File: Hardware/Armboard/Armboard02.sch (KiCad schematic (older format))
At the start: 0 parts

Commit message: H-Bridge completed
Completed the H-Bridge Hierarchal Sheet
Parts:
- added C1: 33nF, symbol Device:C_Small
- added Conn? (x2): AndersonPP, symbol MRDT_Connectors:AndersonPP
- added D1: Zener, symbol Device:D_Zener
- added Gripper_Motor: VNH5019A_E, symbol MRDT_ICs:VNH5019A_E
- added R1, R2, R4, R6, R7, R8: 1k, symbol Device:R
- added R3: 0, symbol Device:R
- added R5: 10k, symbol Device:R
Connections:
- new net: Gripper_Motor.10 (IN_B), R8.2
- new net: Gripper_Motor.4 (IN_A), R1.2
- new net: Gripper_Motor.5 (EN_A/DIAG_A), R2.2
- new net: Gripper_Motor.6 (CS_DIS), R3.2
- new net: Gripper_Motor.7 (PWM), R4.2
- new net: Gripper_Motor.8 (CS), R5.2, R6.1
- new net: Gripper_Motor.9 (EN_B/DIAG_B), R7.2
- new net +12VA: Gripper_Motor.12 (V_BAT), Gripper_Motor.13 (VCC), Gripper_Motor.23 (VCC), Gripper_Motor.3 (VCC), Gripper_Motor.32 (VCC_HEATSLUG)
- new net +3V3: R2.1, R3.1, R7.1
- new net GND: C1.2, D1.2 (A), Gripper_Motor.18 (GND), Gripper_Motor.19 (GND), Gripper_Motor.20 (GND), Gripper_Motor.26 (GND), Gripper_Motor.27 (GND), Gripper_Motor.28 (GND), R6.2
- new net IN_A: R1.1, R8.1
- new net I_SENSE: C1.1, D1.1 (K), R5.1
- new net M_PWM: R4.1
- new net Out_A_M: Conn?.2 (V+Log), Gripper_Motor.1 (OUT_A), Gripper_Motor.25 (OUT_A), Gripper_Motor.30 (OUT_A), Gripper_Motor.31 (OUT_A_HEATSLUG)
- new net Out_B_M: Conn?.1 (GND), Gripper_Motor.15 (OUT_B), Gripper_Motor.16 (OUT_B), Gripper_Motor.21 (OUT_B), Gripper_Motor.33 (OUT_B_HEATSLUG)

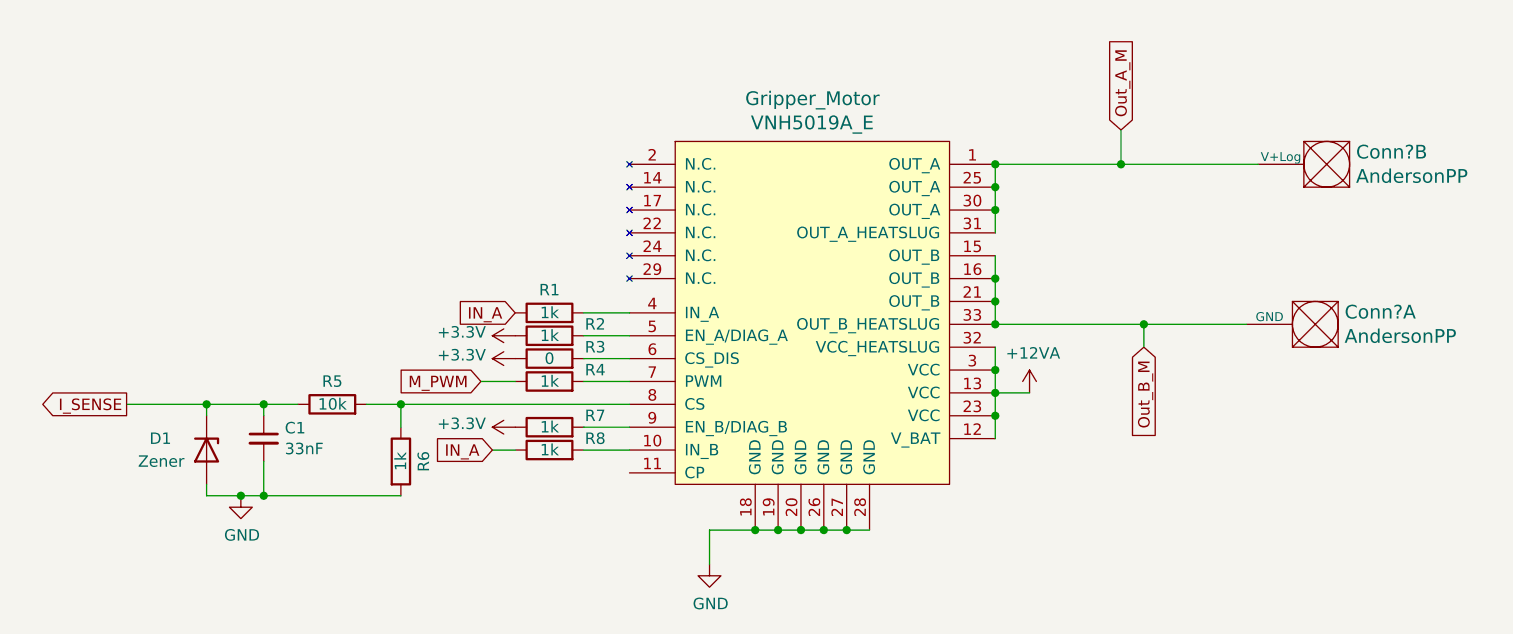
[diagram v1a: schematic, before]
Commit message: Updated H-Bridge
Made the appropriate changes suggested by anthony in slack chat regarding the H-Bridge's flaws
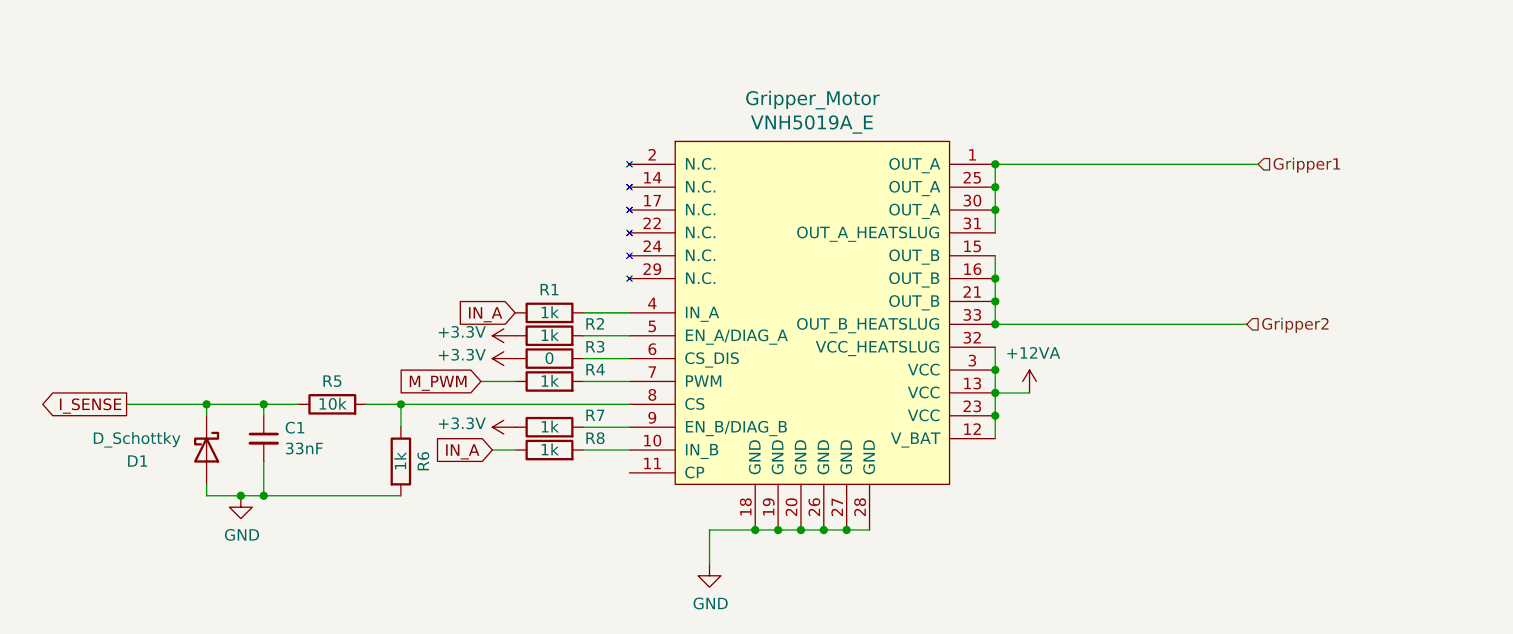
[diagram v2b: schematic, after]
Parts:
- removed Conn? (x2): AndersonPP, symbol MRDT_Connectors:AndersonPP
- removed D1: Zener, symbol Device:D_Zener
- added D_Schottky: D1, symbol Device:D_Schottky
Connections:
- net GND: now also D_Schottky.2 (A)
- net I_SENSE: now also D_Schottky.1 (K)
- net Out_A_M renamed Gripper1
- net Out_B_M renamed Gripper2
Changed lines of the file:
@@
 Wire Wire Line
 	6100 2350 6100 2450
-Wire Wire Line
-	6100 2150 6650 2150
 Connection ~ 6100 2150
 Wire Wire Line
@@
 Wire Wire Line
 	6100 2750 6100 2850
-Wire Wire Line
-	6100 2850 6750 2850
-Connection ~ 6100 2850
 Wire Wire Line
 	6100 2950 6100 3050
@@
 	1    0    0    -1
 $EndComp
-Text GLabel 6650 2000 1    50   Input ~ 0
-Out_A_M
-Wire Wire Line
-	6650 2000 6650 2150
-Connection ~ 6650 2150
-Wire Wire Line
-	6650 2150 7250 2150
-$Comp
-L MRDT_Connectors:AndersonPP Conn?
-U 2 1 5F7FDECE
-P 7650 2250
-F 0 "Conn?" H 7622 2403 60  0000 R CNN
-F 1 "AndersonPP" H 7622 2297 60  0000 R CNN
-F 2 "" H 7500 1700 60  0001 C CNN
-F 3 "" H 7500 1700 60  0001 C CNN
-	2    7650 2250
-	-1   0    0    -1
-$EndComp
-$Comp
-L MRDT_Connectors:AndersonPP Conn?
-U 1 1 5F7FEB3C
-P 7600 2950
-F 0 "Conn?" H 7572 3103 60  0000 R CNN
-F 1 "AndersonPP" H 7572 2997 60  0000 R CNN
-F 2 "" H 7450 2400 60  0001 C CNN
-F 3 "" H 7450 2400 60  0001 C CNN
-	1    7600 2950
-	-1   0    0    -1
-$EndComp
-Text GLabel 6750 2950 3    50   Input ~ 0
-Out_B_M
-Wire Wire Line
-	6750 2950 6750 2850
-Connection ~ 6750 2850
-Wire Wire Line
-	6750 2850 7200 2850
 Wire Wire Line
 	4500 2800 4300 2800
@@
 Wire Wire Line
 	4300 3100 4500 3100
-Text GLabel 3850 3100 0    50   Input ~ 0
-M_PWM
-Text GLabel 4000 2800 0    50   Input ~ 0
-IN_A
 $Comp
 L Device:R R5
@@
 	2650 3600 2650 3550
 Connection ~ 2800 3600
-$Comp
-L Device:D_Zener D1
-U 1 1 5F80F516
-P 2650 3400
-F 0 "D1" V 2600 3150 50  0000 L CNN
-F 1 "Zener" V 2700 3100 50  0000 L CNN
-F 2 "" H 2650 3400 50  0001 C CNN
-F 3 "~" H 2650 3400 50  0001 C CNN
-	1    2650 3400
-	0    1    1    0
-$EndComp
 Text GLabel 2300 3200 0    50   Output ~ 0
 I_SENSE
@@
 	0    -1   -1   0
 $EndComp
+Wire Wire Line
+	3500 3200 4500 3200
+$Comp
+L Device:D_Schottky D_Schottky
+U 1 1 5F84D0E8
+P 2650 3400
+F 0 "D_Schottky" V 2600 2900 50  0000 L CNN
+F 1 "D1" V 2700 3050 50  0000 L CNN
+F 2 "" H 2650 3400 50  0001 C CNN
+F 3 "~" H 2650 3400 50  0001 C CNN
+	1    2650 3400
+	0    1    1    0
+$EndComp
+Wire Wire Line
+	6100 2150 7250 2150
+Connection ~ 6100 2850
+Wire Wire Line
+	6100 2850 7200 2850
+Wire Wire Line
+	3850 3100 4000 3100
+Wire Wire Line
+	4000 3400 3900 3400
 Text GLabel 3900 3400 0    50   Input ~ 0
 IN_A
-Wire Wire Line
-	3500 3200 4500 3200
-Wire Wire Line
-	3850 3100 4000 3100
-Wire Wire Line
-	4000 3400 3900 3400
+Text GLabel 4000 2800 0    50   Input ~ 0
+IN_A
+Text GLabel 3850 3100 0    50   Input ~ 0
+M_PWM
+Text HLabel 7250 2150 2    50   Input ~ 0
+Gripper1
+Text HLabel 7200 2850 2    50   Input ~ 0
+Gripper2
 $EndSCHEMATC

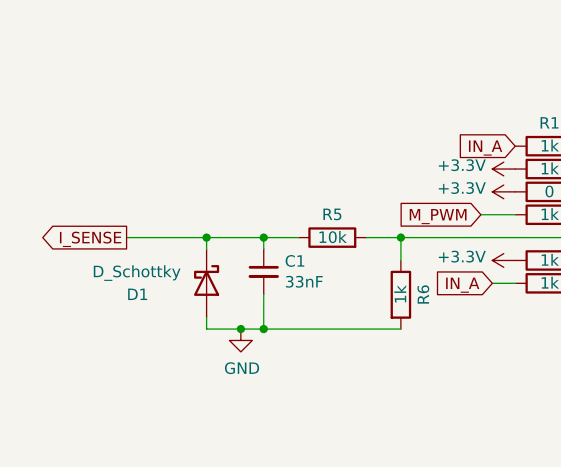
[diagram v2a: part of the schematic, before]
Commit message: Zener fix
Replaced the schotkey diode or however you spell it, with the zener diode
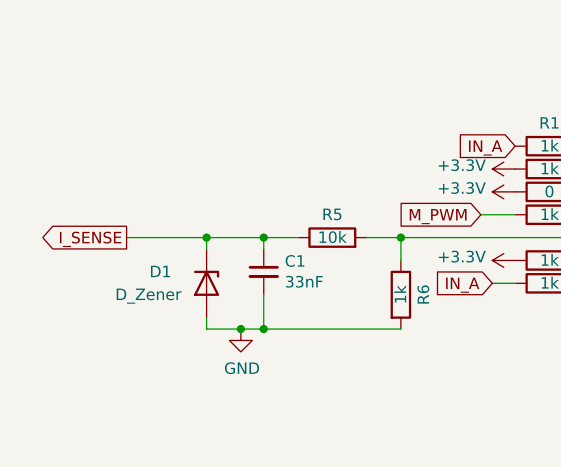
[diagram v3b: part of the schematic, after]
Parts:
- removed D_Schottky: D1, symbol Device:D_Schottky
- added D1: D_Zener, symbol Device:D_Zener
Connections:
- net GND: now also D1.2 (A)
- net I_SENSE: now also D1.1 (K)
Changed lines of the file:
@@
 Wire Wire Line
 	3500 3200 4500 3200
-$Comp
-L Device:D_Schottky D_Schottky
-U 1 1 5F84D0E8
-P 2650 3400
-F 0 "D_Schottky" V 2600 2900 50  0000 L CNN
-F 1 "D1" V 2700 3050 50  0000 L CNN
-F 2 "" H 2650 3400 50  0001 C CNN
-F 3 "~" H 2650 3400 50  0001 C CNN
-	1    2650 3400
-	0    1    1    0
-$EndComp
 Wire Wire Line
 	6100 2150 7250 2150
@@
 Text HLabel 7200 2850 2    50   Input ~ 0
 Gripper2
+$Comp
+L Device:D_Zener D1
+U 1 1 5F8E563D
+P 2650 3400
+F 0 "D1" V 2600 3150 50  0000 L CNN
+F 1 "D_Zener" V 2700 3000 50  0000 L CNN
+F 2 "" H 2650 3400 50  0001 C CNN
+F 3 "~" H 2650 3400 50  0001 C CNN
+	1    2650 3400
+	0    1    1    0
+$EndComp
 $EndSCHEMATC

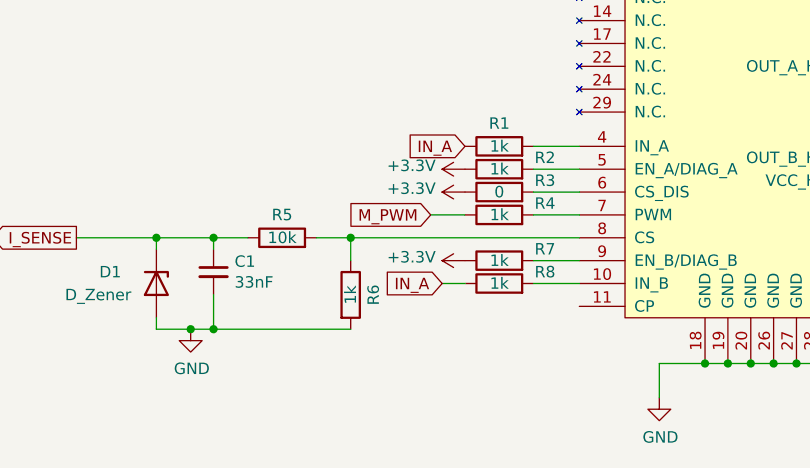
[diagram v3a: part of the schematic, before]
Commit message: Review 2 board changes
-Connected the busses on the power and H-Bridge
-Changed the resistor value to 1.2k
-Fixed some of the pin locations on the TIVA
-Added ferrites to the H-Bridge
-Connected the buses so that they all highlight correctly
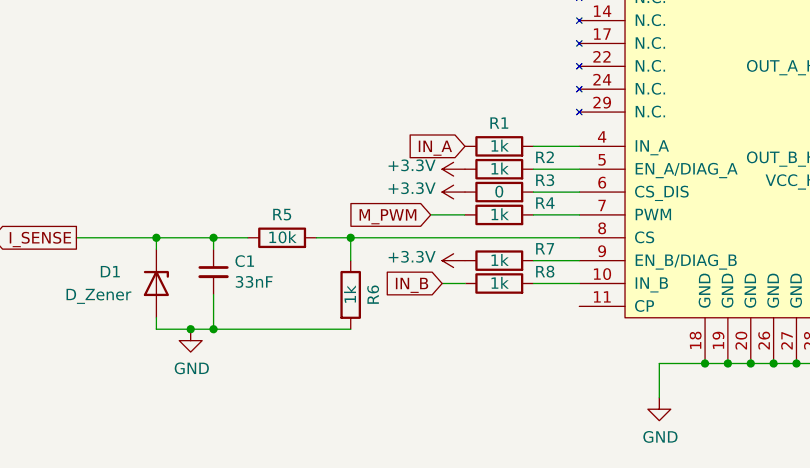
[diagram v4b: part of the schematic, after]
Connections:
- net IN_A: no longer R8.1
- new net IN_B: R8.1
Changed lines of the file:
@@
 $Descr A 11000 8500
 encoding utf-8
-Sheet 3 9
+Sheet 9 9
 Title ""
 Date ""
@@
 	4000 3400 3900 3400
 Text GLabel 3900 3400 0    50   Input ~ 0
-IN_A
+IN_B
 Text GLabel 4000 2800 0    50   Input ~ 0
 IN_A

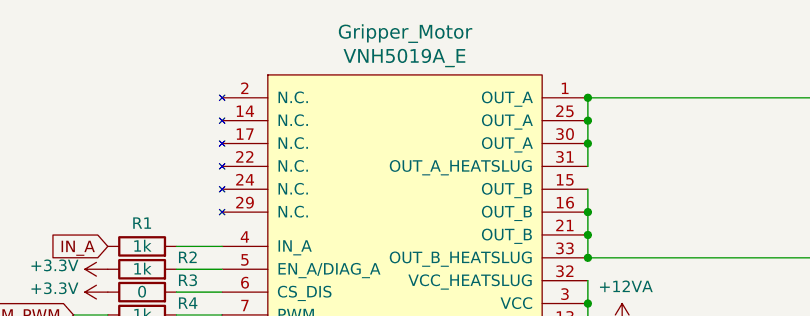
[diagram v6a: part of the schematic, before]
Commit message: Assigned R/L/C footprints
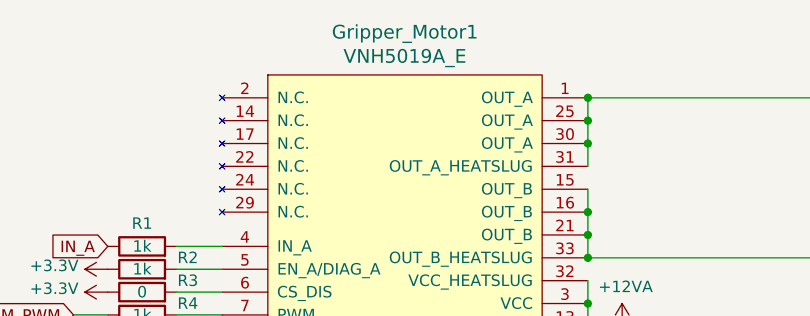
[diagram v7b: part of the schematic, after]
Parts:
- C1: footprint (none) -> Capacitor_SMD:C_0603_1608Metric_Pad1.05x0.95mm_HandSolder
- R1, R2, R3, R4, R5, R6, R7, R8: footprint (none) -> Resistor_SMD:R_0603_1608Metric_Pad1.05x0.95mm_HandSolder
- renumbered Gripper_Motor to Gripper_Motor1
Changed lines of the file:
@@
 $EndDescr
 $Comp
-L MRDT_ICs:VNH5019A_E Gripper_Motor
+L MRDT_ICs:VNH5019A_E Gripper_Motor1
 U 1 1 5F7F9831
 P 4700 3550
-F 0 "Gripper_Motor" H 5300 5237 60  0000 C CNN
+F 0 "Gripper_Motor1" H 5300 5237 60  0000 C CNN
 F 1 "VNH5019A_E" H 5300 5131 60  0000 C CNN
 F 2 "" H 4700 4850 60  0001 C CNN
@@
 $EndComp
 $Comp
-L power:GND #PWR?
+L power:GND #PWR074
 U 1 1 5F7FB309
 P 4850 3900
-F 0 "#PWR?" H 4850 3650 50  0001 C CNN
+F 0 "#PWR074" H 4850 3650 50  0001 C CNN
 F 1 "GND" H 4855 3727 50  0000 C CNN
 F 2 "" H 4850 3900 50  0001 C CNN
@@
 	6100 3150 6250 3150
 $Comp
-L power:+12VA #PWR?
+L power:+12VA #PWR075
 U 1 1 5F7FD222
 P 6250 3150
-F 0 "#PWR?" H 6250 3000 50  0001 C CNN
+F 0 "#PWR075" H 6250 3000 50  0001 C CNN
 F 1 "+12VA" H 6265 3323 50  0000 C CNN
 F 2 "" H 6250 3150 50  0001 C CNN
@@
 	4500 3400 4300 3400
 $Comp
-L power:+3.3V #PWR?
+L power:+3.3V #PWR071
 U 1 1 5F802765
 P 4000 2900
-F 0 "#PWR?" H 4000 2750 50  0001 C CNN
+F 0 "#PWR071" H 4000 2750 50  0001 C CNN
 F 1 "+3.3V" V 4015 3028 50  0000 L CNN
 F 2 "" H 4000 2900 50  0001 C CNN
@@
 F 0 "R1" V 4250 2800 50  0000 C CNN
 F 1 "1k" V 4150 2800 50  0000 C CNN
-F 2 "" V 4080 2800 50  0001 C CNN
+F 2 "Resistor_SMD:R_0603_1608Metric_Pad1.05x0.95mm_HandSolder" V 4080 2800 50  0001 C CNN
 F 3 "~" H 4150 2800 50  0001 C CNN
 	1    4150 2800
@@
 F 0 "R2" V 4200 2700 50  0000 C CNN
 F 1 "1k" V 4150 2900 50  0000 C CNN
-F 2 "" V 4080 2900 50  0001 C CNN
+F 2 "Resistor_SMD:R_0603_1608Metric_Pad1.05x0.95mm_HandSolder" V 4080 2900 50  0001 C CNN
 F 3 "~" H 4150 2900 50  0001 C CNN
 	1    4150 2900
@@
 F 0 "R3" V 4200 2800 50  0000 C CNN
 F 1 "0" V 4150 3000 50  0000 C CNN
-F 2 "" V 4080 3000 50  0001 C CNN
+F 2 "Resistor_SMD:R_0603_1608Metric_Pad1.05x0.95mm_HandSolder" V 4080 3000 50  0001 C CNN
 F 3 "~" H 4150 3000 50  0001 C CNN
 	1    4150 3000
@@
 F 0 "R4" V 4200 2900 50  0000 C CNN
 F 1 "1k" V 4150 3100 50  0000 C CNN
-F 2 "" V 4080 3100 50  0001 C CNN
+F 2 "Resistor_SMD:R_0603_1608Metric_Pad1.05x0.95mm_HandSolder" V 4080 3100 50  0001 C CNN
 F 3 "~" H 4150 3100 50  0001 C CNN
 	1    4150 3100
@@
 $EndComp
 $Comp
-L power:+3.3V #PWR?
+L power:+3.3V #PWR072
 U 1 1 5F807CCC
 P 4000 3000
-F 0 "#PWR?" H 4000 2850 50  0001 C CNN
+F 0 "#PWR072" H 4000 2850 50  0001 C CNN
 F 1 "+3.3V" V 4015 3128 50  0000 L CNN
 F 2 "" H 4000 3000 50  0001 C CNN
@@
 F 0 "R5" V 3300 3200 50  0000 C CNN
 F 1 "10k" V 3200 3200 50  0000 C CNN
-F 2 "" V 3130 3200 50  0001 C CNN
+F 2 "Resistor_SMD:R_0603_1608Metric_Pad1.05x0.95mm_HandSolder" V 3130 3200 50  0001 C CNN
 F 3 "~" H 3200 3200 50  0001 C CNN
 	1    3200 3200
@@
 F 0 "R6" V 3600 3450 50  0000 C CNN
 F 1 "1k" V 3500 3450 50  0000 C CNN
-F 2 "" V 3430 3450 50  0001 C CNN
+F 2 "Resistor_SMD:R_0603_1608Metric_Pad1.05x0.95mm_HandSolder" V 3430 3450 50  0001 C CNN
 F 3 "~" H 3500 3450 50  0001 C CNN
 	1    3500 3450
@@
 F 0 "C1" H 2992 3396 50  0000 L CNN
 F 1 "33nF" H 2992 3305 50  0000 L CNN
-F 2 "" H 2900 3350 50  0001 C CNN
+F 2 "Capacitor_SMD:C_0603_1608Metric_Pad1.05x0.95mm_HandSolder" H 2900 3350 50  0001 C CNN
 F 3 "~" H 2900 3350 50  0001 C CNN
 	1    2900 3350
@@
 	2900 3200 2900 3250
 $Comp
-L power:GND #PWR?
+L power:GND #PWR070
 U 1 1 5F80DDCF
 P 2800 3600
-F 0 "#PWR?" H 2800 3350 50  0001 C CNN
+F 0 "#PWR070" H 2800 3350 50  0001 C CNN
 F 1 "GND" H 2805 3427 50  0000 C CNN
 F 2 "" H 2800 3600 50  0001 C CNN
@@
 F 0 "R7" V 4200 3100 50  0000 C CNN
 F 1 "1k" V 4150 3300 50  0000 C CNN
-F 2 "" V 4080 3300 50  0001 C CNN
+F 2 "Resistor_SMD:R_0603_1608Metric_Pad1.05x0.95mm_HandSolder" V 4080 3300 50  0001 C CNN
 F 3 "~" H 4150 3300 50  0001 C CNN
 	1    4150 3300
@@
 F 0 "R8" V 4200 3200 50  0000 C CNN
 F 1 "1k" V 4150 3400 50  0000 C CNN
-F 2 "" V 4080 3400 50  0001 C CNN
+F 2 "Resistor_SMD:R_0603_1608Metric_Pad1.05x0.95mm_HandSolder" V 4080 3400 50  0001 C CNN
 F 3 "~" H 4150 3400 50  0001 C CNN
 	1    4150 3400
@@
 $EndComp
 $Comp
-L power:+3.3V #PWR?
+L power:+3.3V #PWR073
 U 1 1 5F818EFA
 P 4000 3300
-F 0 "#PWR?" H 4000 3150 50  0001 C CNN
+F 0 "#PWR073" H 4000 3150 50  0001 C CNN
 F 1 "+3.3V" V 4015 3428 50  0000 L CNN
 F 2 "" H 4000 3300 50  0001 C CNN

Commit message: Added more footprints
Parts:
- D1: footprint (none) -> Diode_SMD:D_SOD-323_HandSoldering
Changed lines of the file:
@@
 F 0 "D1" V 2600 3150 50  0000 L CNN
 F 1 "D_Zener" V 2700 3000 50  0000 L CNN
-F 2 "" H 2650 3400 50  0001 C CNN
+F 2 "Diode_SMD:D_SOD-323_HandSoldering" H 2650 3400 50  0001 C CNN
 F 3 "~" H 2650 3400 50  0001 C CNN
 	1    2650 3400
